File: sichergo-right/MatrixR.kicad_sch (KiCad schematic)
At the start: 72 parts, among them SW17 SW_Push, SW18 SW_Push, SW22 SW_Push, SW23 SW_Push, SW24 SW_Push, SW25 SW_Push, SW26 SW_Push, SW27 SW_Push, SW28 SW_Push, SW29 SW_Push, SW30 SW_Push, SW31 SW_Push, SW32 SW_Push, SW33 SW_Push, SW34 SW_Push, SW35 SW_Push, SW36 SW_Push, SW37 SW_Push

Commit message: Split design in two PCBs and remake layout
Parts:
- renumbered D41 to D1, D50 to D10, D42 to D11, D39 to D12, D23 to D13, D24 to D14, D25 to D15, D33 to D16, D54 to D17, D49 to D18, D43 to D19, D38 to D2, D40 to D20, D26 to D21, D27 to D22, D28 to D23, D37 to D24, D55 to D25, D48 to D26, D44 to D27, D30 to D28, D31 to D29, D52 to D3, D32 to D30, D47 to D31, D46 to D32, D45 to D33, D51 to D4, D17 to D5, D18 to D6, D22 to D7, D29 to D8, D53 to D9, R32 to R10, R24 to R11, R31 to R12, R25 to R13, R22 to R14, R16 to R15, R30 to R16, R26 to R17, R20 to R18, R17 to R19, R29 to R20, R18 to R22, R28 to R23, R27 to R24, R19 to R25, R23 to R8, R15 to R9, SW17 to SW1, SW27 to SW10, SW28 to SW11, SW37 to SW12, SW30 to SW13, SW31 to SW14, SW32 to SW15, SW34 to SW16, SW35 to SW17, SW36 to SW18, SW18 to SW2, SW22 to SW3, SW29 to SW4, SW23 to SW5, SW24 to SW6, SW25 to SW7, SW33 to SW8, SW26 to SW9

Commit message: Remake entire shape
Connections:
- net KB_ROW_4 renamed KB_ROW_0
- net KB_ROW_5 renamed KB_ROW_1
- net KB_ROW_6 renamed KB_ROW_2
- net KB_ROW_7 renamed KB_ROW_3
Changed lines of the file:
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@@
 		)
 	)
-	(hierarchical_label "KB_ROW_7"
+	(hierarchical_label "KB_ROW_3"
 		(shape output)
 		(at 85.09 138.43 180)
@@
 		)
 	)
-	(hierarchical_label "KB_ROW_4"
+	(hierarchical_label "KB_ROW_0"
 		(shape output)
 		(at 85.09 69.85 180)
@@
 		)
 	)
-	(hierarchical_label "KB_ROW_5"
+	(hierarchical_label "KB_ROW_1"
 		(shape output)
 		(at 85.09 91.44 180)
@@
 		)
 	)
-	(hierarchical_label "KB_ROW_6"
+	(hierarchical_label "KB_ROW_2"
 		(shape output)
 		(at 85.09 114.3 180)

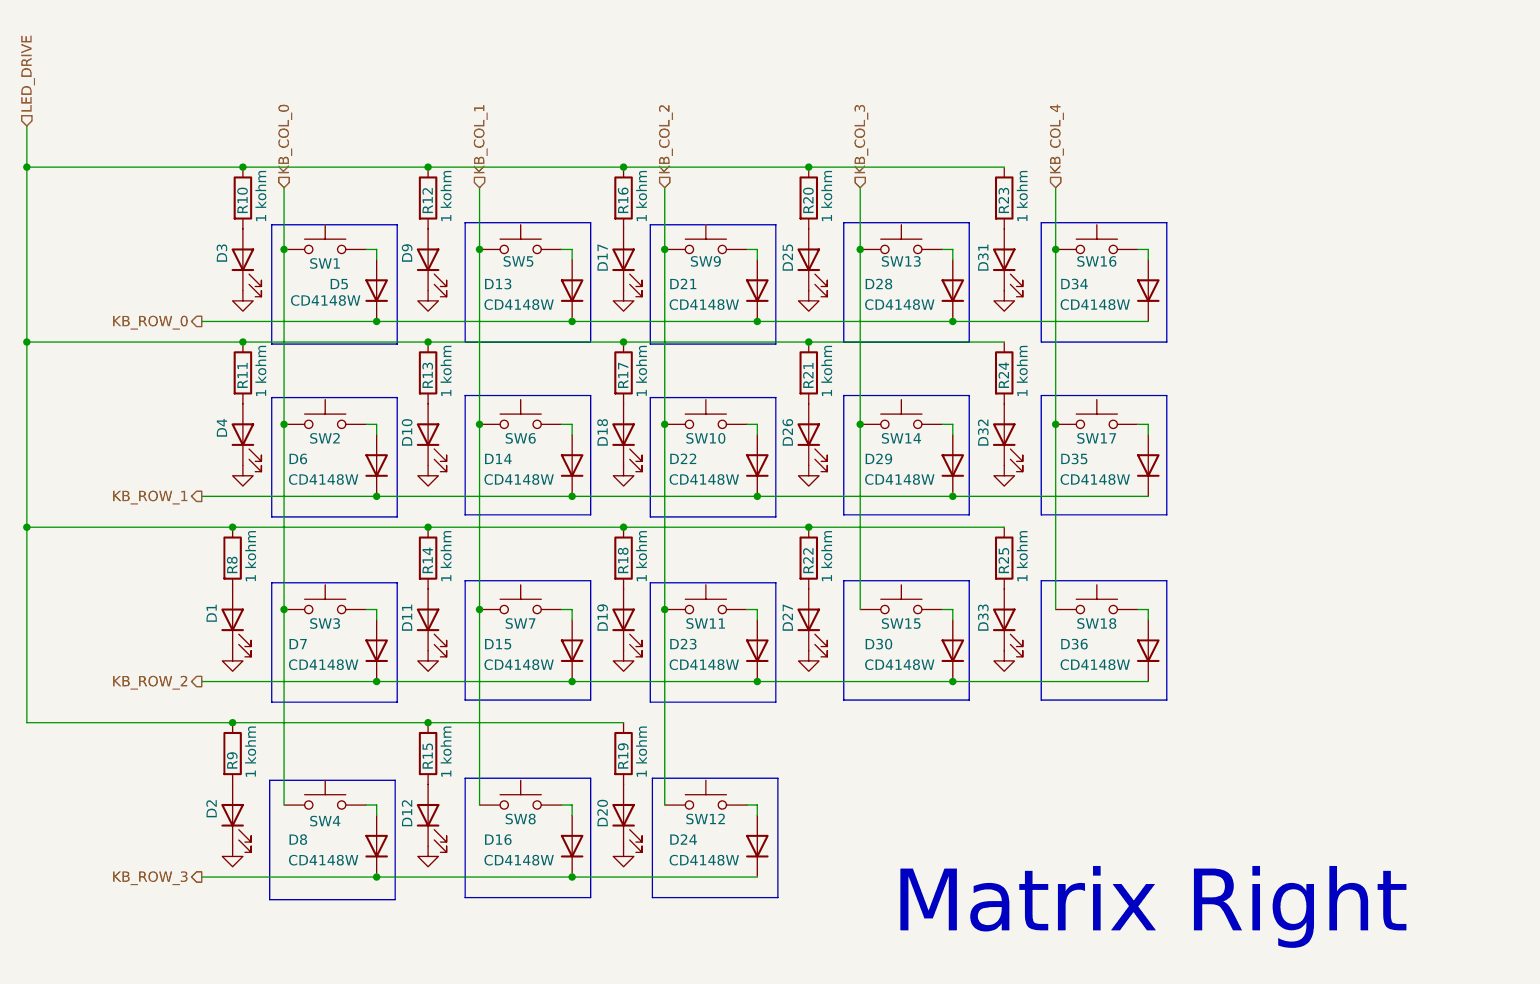
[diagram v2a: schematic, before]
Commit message: Fix keyboard layout size
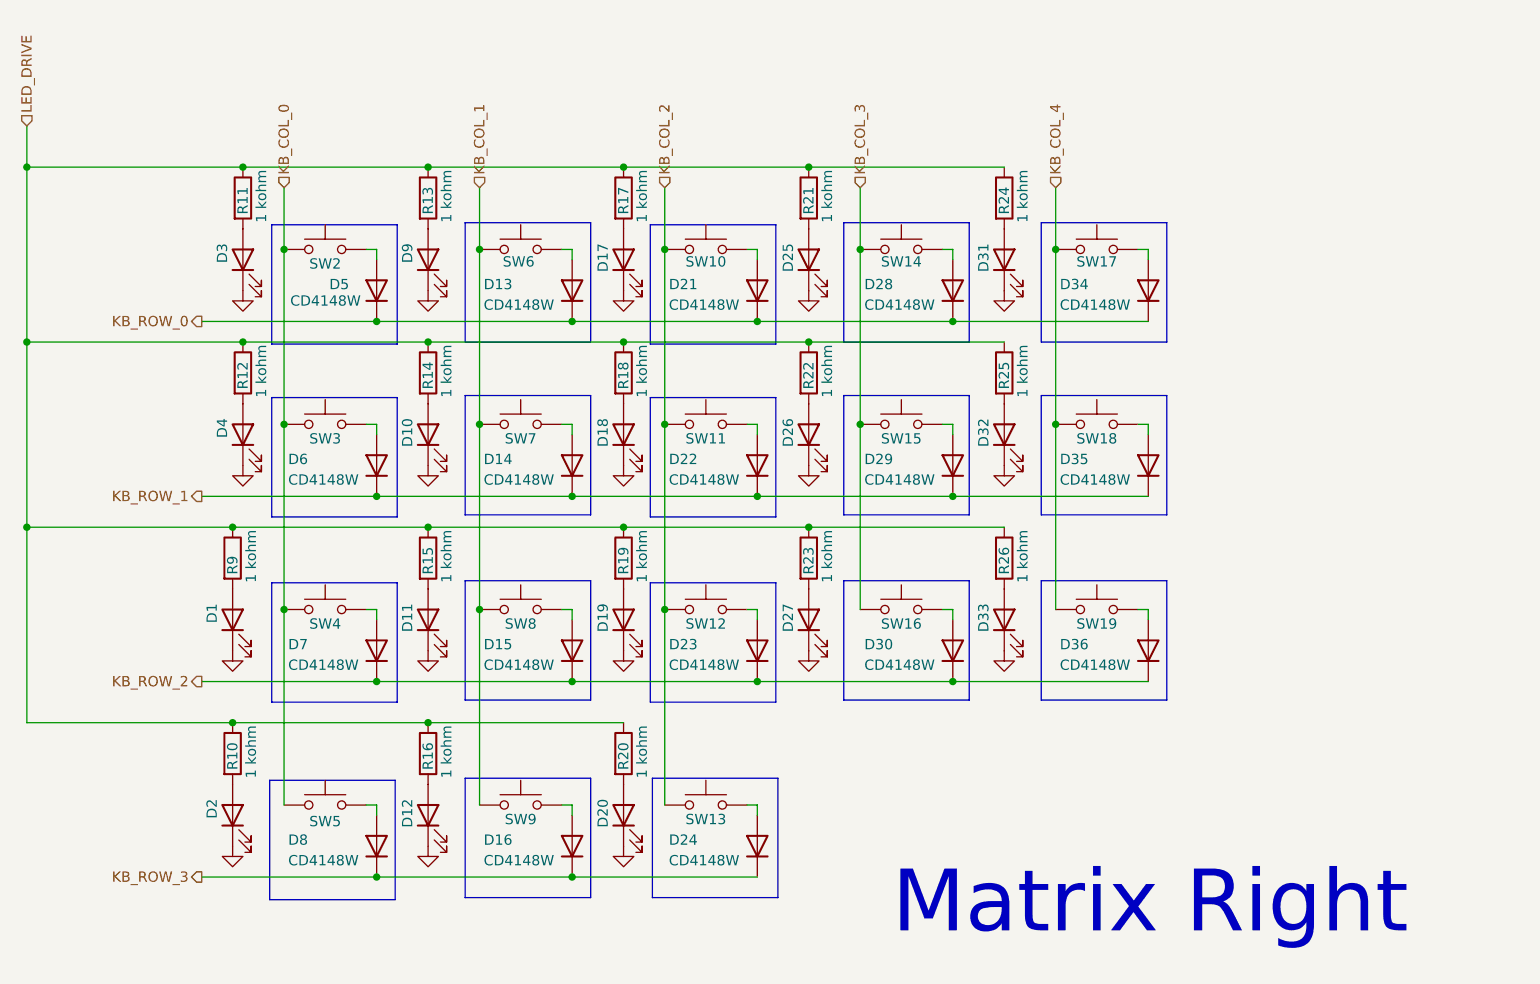
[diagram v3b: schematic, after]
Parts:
- renumbered R9 to R10, R10 to R11, R11 to R12, R12 to R13, R13 to R14, R14 to R15, R15 to R16, R16 to R17, R17 to R18, R18 to R19, R19 to R20, R20 to R21, R21 to R22, R22 to R23, R23 to R24, R24 to R25, R25 to R26, R8 to R9, SW9 to SW10, SW10 to SW11, SW11 to SW12, SW12 to SW13, SW13 to SW14, SW14 to SW15, SW15 to SW16, SW16 to SW17, SW17 to SW18, SW18 to SW19, SW1 to SW2, SW2 to SW3, SW3 to SW4, SW4 to SW5, SW5 to SW6, SW6 to SW7, SW7 to SW8, SW8 to SW9
